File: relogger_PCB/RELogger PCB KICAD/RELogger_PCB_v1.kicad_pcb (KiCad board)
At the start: 2 copper layers, 73 parts, among them J1 RTC_MODULE, J2 Arduino_Nano_Header, J3 MICRO_SD, K1 ANEMOM1, P1 EXTERNAL PSU, P10 VANE, P11 SERIAL, P12 SOFT_SERIAL, P13 D6_D7, P14 AC_IN, P15 ANEMOM2, P2 BATTERY, P22 A_IN_45, P23 AGND_GND, P26 JMP_HALL, P3 SOLAR, P4 A_IN_01, P5 A_IN_23, P6 I2C_1, P7 I2C_2, P8 V_EXT, P9 3V3_VREF, Q2 RFU9110PBF, SW1 CALIBRATE, SW2 SW_PUSH_SMALL_H, SW3 ON/OFF, SW4 SW_PUSH_SMALL_H, U1 MCP3208, U2 MCP1826S, U3 LM2574, U5 MCP73832, U6 LM393

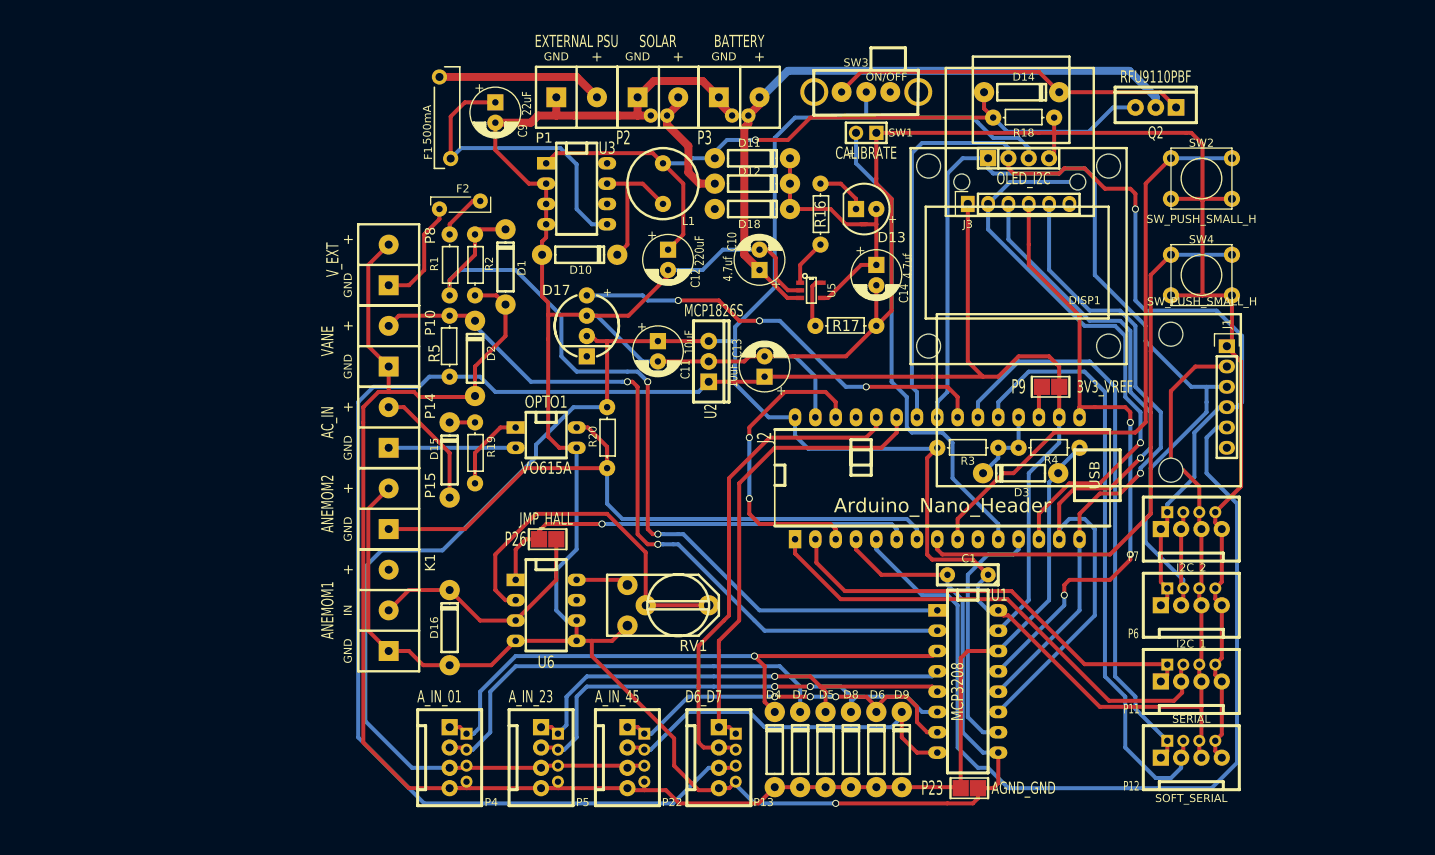
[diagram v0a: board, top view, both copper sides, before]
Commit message: Re load of new PCB
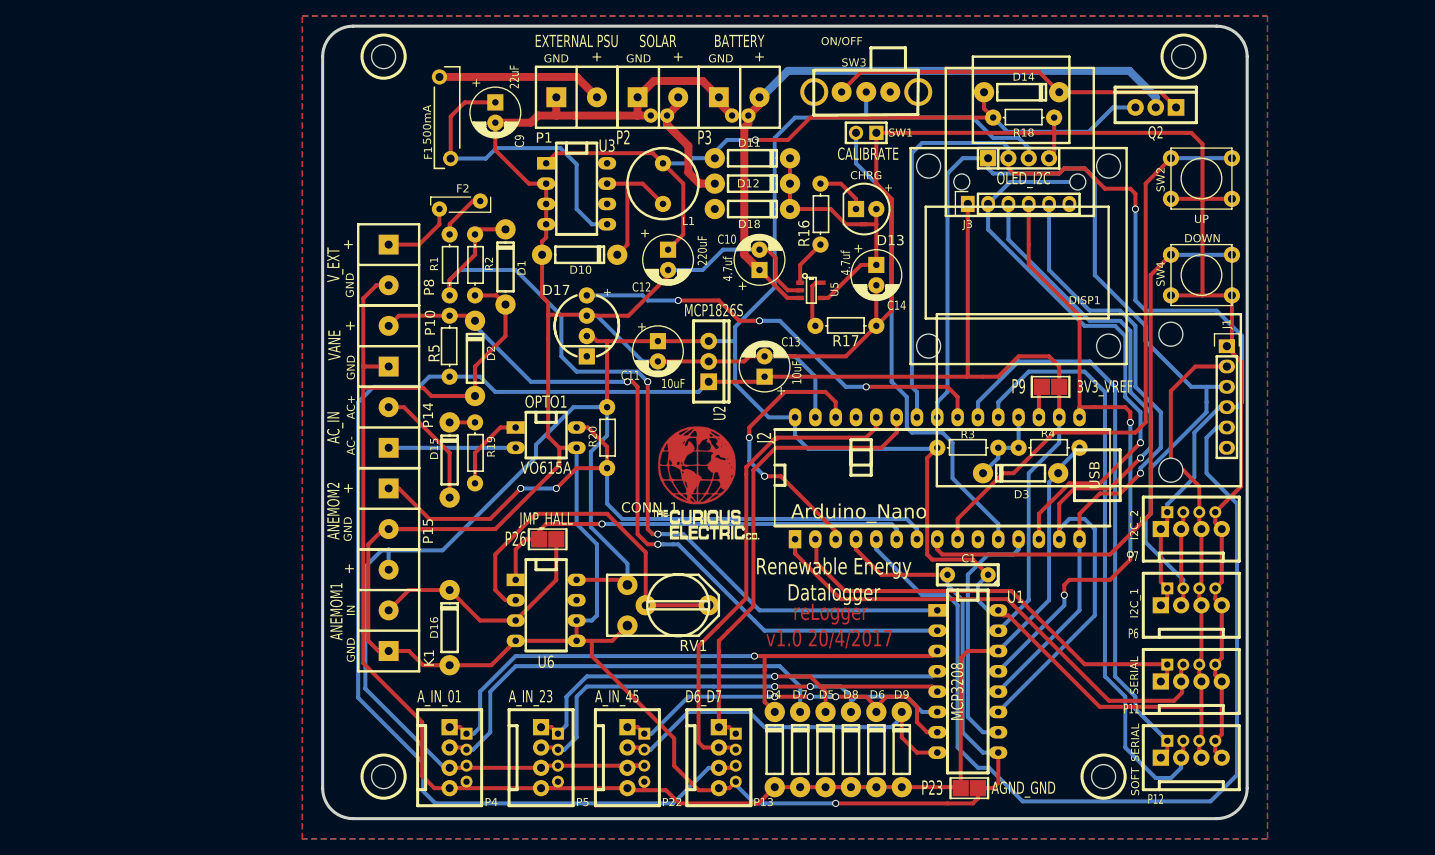
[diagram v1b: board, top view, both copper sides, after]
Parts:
- added HOLE1: CONN_1, 3mm_hole_relogger, F.Cu at (85.1, 36.8)
- added LOGO1: CONN_1, CuriousElectric3:CEC_Globe_10mm_FCU, F.Cu at (124.3, 87.9)
- added LOGO2: CONN_1, CuriousElectric3:TCEC_Words_13mm, F.Cu at (118.4, 93.2)
- J2: value Arduino_Nano_Header -> Arduino_Nano
- SW2: value SW_PUSH_SMALL_H -> UP
- SW4: value SW_PUSH_SMALL_H -> DOWN
- moved P15 5.08 mm to (85.7, 90.8), turned to 270 degrees
- moved P8 5.08 mm to (85.7, 60.3), turned to 270 degrees
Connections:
- K1 pad 3: (no net) -> /Vss
- RV1 pad 1: /Hall_to_freq/Vss -> /Vss
- U6 pad 8: /Hall_to_freq/Vss -> /Vss
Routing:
- net /Vss: track 342.5 -> 376.6 mm
- net GND: track 544.3 -> 576.4 mm
- net /Hall_to_freq/Vss: track 6.61 -> 0.00 mm
- net Net-(F2-Pad1): track 13.6 -> 9.31 mm
- net /Arduino Uno/RESET: track 38.7 -> 34.7 mm
- net /CLK_INT: track 115.7 -> 118.0 mm
- net GNDA: track 227.9 -> 225.9 mm
- net +3.3V: track 245.1 -> 243.6 mm
- net /IN_ACFREQ: track 83.7 -> 84.8 mm, vias 0 -> 2
- net /A0: track 76.7 -> 76.2 mm
- added copper zone on B.Cu, net GND
- added copper zone on F.Cu, net GND
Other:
- board outline added: 115.6 x 99.1 mm
- board text added: "Renewable Energy Datalogger"
- board text added: "reLogger"
- board text added: "v1.0 20/4/2017"

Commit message: BOM updated
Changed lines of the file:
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@@
       (effects (font (thickness 0.3)))
     )
-    (fp_text value CONN_1 (at 0 0) (layer F.SilkS)
+    (fp_text value CONN_1 (at 0 0) (layer F.SilkS) hide
       (effects (font (thickness 0.15)))
     )

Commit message: update of PCB
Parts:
- J2: value Arduino_Nano -> Arduino_Nano_Header
- SW2: value UP -> SW_PUSH_SMALL_H
- SW4: value DOWN -> SW_PUSH_SMALL_H
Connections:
- J3 pad 6: (no net) -> GND
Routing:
- net GND: track 576.4 -> 583.2 mm, vias 1 -> 2
- net /SDA: track 130.3 -> 132.1 mm
- net /SCLK: track 134.7 -> 134.0 mm
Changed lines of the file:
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@@
 (kicad_pcb (version 4) (host pcbnew 4.0.4-stable)
   (general
-    (links 217)
+    (links 218)
     (no_connects 0)
-    (area 74.93 31.75 195.580001 134.620001)
+    (area 77.279499 32.829499 193.230501 132.270501)
     (thickness 1.6002)
     (drawings 11)
-    (tracks 917)
+    (tracks 923)
     (zones 0)
     (modules 76)
@@
       (effects (font (size 1.778 1.143) (thickness 0.3048)))
     )
-    (fp_text value Arduino_Nano (at -16.129 4.191) (layer F.SilkS)
+    (fp_text value Arduino_Nano_Header (at -16.129 4.191) (layer F.SilkS)
       (effects (font (size 1.778 1.778) (thickness 0.3048)))
     )
@@
       (effects (font (size 1.016 1.016) (thickness 0.2032)))
     )
-    (fp_text value UP (at 0 5.08) (layer F.SilkS)
+    (fp_text value SW_PUSH_SMALL_H (at 0 5.08) (layer F.SilkS)
       (effects (font (size 1.016 1.016) (thickness 0.2032)))
     )
@@
       (effects (font (size 1.016 1.016) (thickness 0.2032)))
     )
-    (fp_text value DOWN (at 0.127 -4.572) (layer F.SilkS)
+    (fp_text value SW_PUSH_SMALL_H (at 0.127 -4.572) (layer F.SilkS)
       (effects (font (size 1.016 1.016) (thickness 0.2032)))
     )
@@
     (pad 5 thru_hole oval (at 0 10.16 90) (size 2.032 1.7272) (drill 1.016) (layers *.Cu *.Mask F.SilkS)
       (net 44 /DOUT_ADC))
-    (pad 6 thru_hole oval (at 0 12.7 90) (size 2.032 1.7272) (drill 1.016) (layers *.Cu *.Mask F.SilkS))
+    (pad 6 thru_hole oval (at 0 12.7 90) (size 2.032 1.7272) (drill 1.016) (layers *.Cu *.Mask F.SilkS)
+      (net 4 GND))
     (pad "" np_thru_hole circle (at 2.75 -0.75 90) (size 2 2) (drill 2) (layers *.Cu *.Mask))
     (pad 2 np_thru_hole circle (at 2.75 13.75 90) (size 2 2) (drill 2) (layers *.Cu *.Mask)
@@
   (segment (start 121.92 41.91) (end 121.92 42.799) (width 1) (layer Front) (net 3))
   (segment (start 121.92 42.799) (end 120.523 44.196) (width 1) (layer Front) (net 3))
+  (segment (start 168.275 49.53) (end 168.275 51.943) (width 0.5) (layer Back) (net 4) (status 400000))
+  (segment (start 168.275 51.943) (end 170.815 54.483) (width 0.5) (layer Front) (net 4) (status 800000))
+  (via (at 168.275 51.943) (size 0.889) (drill 0.635) (layers Front Back) (net 4))
+  (segment (start 170.815 54.483) (end 170.815 55.245) (width 0.5) (layer Front) (net 4) (status C00000))
   (segment (start 109.22 107.315) (end 111.125 107.315) (width 0.5) (layer Back) (net 4))
   (segment (start 111.76 97.79) (end 109.22 95.25) (width 0.5) (layer Back) (net 4))
@@
   (segment (start 155.575 78.105) (end 145.415 78.105) (width 0.5) (layer Front) (net 27))
   (segment (start 156.845 79.375) (end 155.575 78.105) (width 0.5) (layer Front) (net 27))
+  (segment (start 160.655 49.53) (end 160.655 51.943) (width 0.5) (layer Back) (net 28) (status 400000))
+  (segment (start 171.069 50.8) (end 171.323 50.8) (width 0.5) (layer Back) (net 28))
+  (segment (start 169.037 52.832) (end 171.069 50.8) (width 0.5) (layer Back) (net 28))
+  (segment (start 161.544 52.832) (end 169.037 52.832) (width 0.5) (layer Back) (net 28))
+  (segment (start 160.655 51.943) (end 161.544 52.832) (width 0.5) (layer Back) (net 28))
   (segment (start 187.96 78.105) (end 187.96 80.01) (width 0.5) (layer Back) (net 28))
   (segment (start 190.5 78.105) (end 187.96 78.105) (width 0.5) (layer Back) (net 28))
   (segment (start 187.96 78.105) (end 186.055 78.105) (width 0.5) (layer Back) (net 28))
-  (segment (start 160.655 50.8) (end 160.655 49.53) (width 0.5) (layer Back) (net 28))
-  (segment (start 161.29 51.435) (end 160.655 50.8) (width 0.5) (layer Back) (net 28))
-  (segment (start 169.545 51.435) (end 161.29 51.435) (width 0.5) (layer Back) (net 28))
-  (segment (start 170.18 50.8) (end 169.545 51.435) (width 0.5) (layer Back) (net 28))
-  (segment (start 172.72 50.8) (end 170.18 50.8) (width 0.5) (layer Back) (net 28))
-  (segment (start 173.99 52.07) (end 172.72 50.8) (width 0.5) (layer Back) (net 28))
-  (segment (start 173.99 64.135) (end 173.99 52.07) (width 0.5) (layer Back) (net 28))
-  (segment (start 180.34 70.485) (end 173.99 64.135) (width 0.5) (layer Back) (net 28))
-  (segment (start 180.34 72.39) (end 180.34 70.485) (width 0.5) (layer Back) (net 28))
   (segment (start 186.055 78.105) (end 180.34 72.39) (width 0.5) (layer Back) (net 28))
+  (segment (start 180.34 72.39) (end 180.34 70.485) (width 0.5) (layer Back) (net 28))
+  (segment (start 180.34 70.485) (end 173.99 64.135) (width 0.5) (layer Back) (net 28))
+  (segment (start 173.99 64.135) (end 173.99 52.07) (width 0.5) (layer Back) (net 28))
+  (segment (start 173.99 52.07) (end 172.72 50.8) (width 0.5) (layer Back) (net 28))
+  (segment (start 172.72 50.8) (end 171.323 50.8) (width 0.5) (layer Back) (net 28))
   (segment (start 180.34 97.536) (end 180.34 94.615) (width 0.5) (layer Back) (net 28))
   (segment (start 185.055 102.251) (end 180.34 97.536) (width 0.5) (layer Back) (net 28))
@@
   (segment (start 185.055 103.299) (end 185.055 105.14) (width 0.5) (layer Front) (net 28))
   (segment (start 185.055 105.14) (end 184.785 105.41) (width 0.5) (layer Front) (net 28))
+  (segment (start 163.195 49.53) (end 163.195 50.546) (width 0.5) (layer Front) (net 29) (status C00000))
+  (segment (start 163.195 50.546) (end 163.576 50.927) (width 0.5) (layer Front) (net 29) (status 400000))
+  (segment (start 172.847 50.927) (end 173.609 51.689) (width 0.5) (layer Front) (net 29))
+  (segment (start 163.576 50.927) (end 172.847 50.927) (width 0.5) (layer Front) (net 29))
   (segment (start 190.5 80.645) (end 191.77 80.645) (width 0.5) (layer Back) (net 29))
-  (segment (start 163.195 50.8) (end 163.195 49.53) (width 0.5) (layer Front) (net 29))
-  (segment (start 163.83 51.435) (end 163.195 50.8) (width 0.5) (layer Front) (net 29))
-  (segment (start 169.545 51.435) (end 163.83 51.435) (width 0.5) (layer Front) (net 29))
-  (segment (start 170.18 50.8) (end 169.545 51.435) (width 0.5) (layer Front) (net 29))
-  (segment (start 172.72 50.8) (end 170.18 50.8) (width 0.5) (layer Front) (net 29))
-  (segment (start 175.26 53.34) (end 172.72 50.8) (width 0.5) (layer Front) (net 29))
+  (segment (start 175.26 53.34) (end 173.609 51.689) (width 0.5) (layer Front) (net 29))
   (segment (start 178.435 53.34) (end 175.26 53.34) (width 0.5) (layer Front) (net 29))
   (segment (start 179.07 53.975) (end 178.435 53.34) (width 0.5) (layer Front) (net 29))
@@
   (segment (start 158.115 119.38) (end 158.115 101.6) (width 0.5) (layer Back) (net 41))
   (segment (start 160.02 121.285) (end 158.115 119.38) (width 0.5) (layer Back) (net 41))
+  (segment (start 160.655 55.245) (end 160.655 54.483) (width 0.5) (layer Back) (net 42) (status C00000))
+  (segment (start 160.655 54.483) (end 161.544 53.594) (width 0.5) (layer Back) (net 42) (status 400000))
+  (segment (start 170.766 53.594) (end 171.865 52.495) (width 0.5) (layer Back) (net 42) (status 800000))
+  (segment (start 161.544 53.594) (end 170.766 53.594) (width 0.5) (layer Back) (net 42))
   (segment (start 160.655 55.245) (end 160.655 58.42) (width 0.5) (layer Back) (net 42))
   (segment (start 167.005 93.98) (end 167.005 97.155) (width 0.5) (layer Front) (net 42))
@@
   (segment (start 172.72 70.485) (end 176.53 70.485) (width 0.5) (layer Back) (net 42))
   (segment (start 160.655 58.42) (end 172.72 70.485) (width 0.5) (layer Back) (net 42))
-  (segment (start 171.865 52.495) (end 163.405 52.495) (width 0.5) (layer Back) (net 42))
-  (segment (start 163.405 52.495) (end 160.655 55.245) (width 0.5) (layer Back) (net 42))
   (segment (start 163.195 55.245) (end 163.195 59.69) (width 0.5) (layer Back) (net 43))
   (segment (start 169.545 92.71) (end 169.545 97.155) (width 0.5) (layer Front) (net 43))
